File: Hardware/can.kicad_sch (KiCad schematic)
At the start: 11 parts, among them U4 SN65HVD230

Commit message: added jumper to change the buck converter to 8.4v
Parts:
- C33, C35, C36, C37: footprint Capacitor_SMD:C_0603_1608Metric -> Capacitor_SMD:C_0402_1005Metric
- JP1: footprint (none) -> Jumper:SolderJumper-2_P1.3mm_Open_RoundedPad1.0x1.5mm
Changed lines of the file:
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@@
       (effects (font (size 1.27 1.27)) (justify right))
     )
-    (property "Footprint" "Capacitor_SMD:C_0603_1608Metric" (id 2) (at 175.26 82.55 0)
+    (property "Footprint" "Capacitor_SMD:C_0402_1005Metric" (id 2) (at 175.26 82.55 0)
       (effects (font (size 1.27 1.27)) hide)
     )
@@
       (effects (font (size 1.27 1.27)) (justify left))
     )
-    (property "Footprint" "Capacitor_SMD:C_0603_1608Metric" (id 2) (at 121.92 71.12 0)
+    (property "Footprint" "Capacitor_SMD:C_0402_1005Metric" (id 2) (at 121.92 71.12 0)
       (effects (font (size 1.27 1.27)) hide)
     )
@@
     (property "Reference" "C35" (id 0) (at 171.45 82.55 90))
     (property "Value" "0.1uF" (id 1) (at 171.45 85.09 90))
-    (property "Footprint" "Capacitor_SMD:C_0603_1608Metric" (id 2) (at 175.26 87.9348 0)
+    (property "Footprint" "Capacitor_SMD:C_0402_1005Metric" (id 2) (at 175.26 87.9348 0)
       (effects (font (size 1.27 1.27)) hide)
     )
@@
     (property "Reference" "JP1" (id 0) (at 157.48 82.55 0))
     (property "Value" "TermJP" (id 1) (at 157.48 85.09 0))
-    (property "Footprint" "" (id 2) (at 157.48 88.9 0)
+    (property "Footprint" "Jumper:SolderJumper-2_P1.3mm_Open_RoundedPad1.0x1.5mm" (id 2) (at 157.48 88.9 0)
       (effects (font (size 1.27 1.27)) hide)
     )
@@
       (effects (font (size 1.27 1.27)) (justify right))
     )
-    (property "Footprint" "Capacitor_SMD:C_0603_1608Metric" (id 2) (at 175.26 100.33 0)
+    (property "Footprint" "Capacitor_SMD:C_0402_1005Metric" (id 2) (at 175.26 100.33 0)
       (effects (font (size 1.27 1.27)) hide)
     )

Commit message: End of V1
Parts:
- removed JP1: TermJP, Jumper:SolderJumper-2_P1.3mm_Open_RoundedPad1.0x1.5mm, symbol Jumper:SolderJumper_2_Open
- added C32: 160pF, Capacitor_SMD:C_0603_1608Metric, symbol Device:C_Small
- added R26, R27: 90, Resistor_SMD:R_0603_1608Metric, symbol Device:R_Small
- added R33: 0, Resistor_SMD:R_0603_1608Metric, symbol Device:R_Small
- C33, C35, C36, C37: footprint Capacitor_SMD:C_0402_1005Metric -> Capacitor_SMD:C_0603_1608Metric
- R29, R30: footprint Resistor_SMD:R_0603_1608Metric -> Resistor_SMD:R_0805_2012Metric
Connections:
- net CAN_RX: now also R27.1; no longer U4.4 (R)
- net CAN_TX: now also R26.1; no longer U4.1 (D)
- net GND: now also C32.1
- net Vref: now also R33.1
- net at C35.1, R29.2, R30.1: now also R33.2
- new net: C32.2, R26.2, U4.1 (D)
- new net: R27.2, U4.4 (R)
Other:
- moved on the sheet: C33, C34, C35, C36, C37, D12, R29, R30

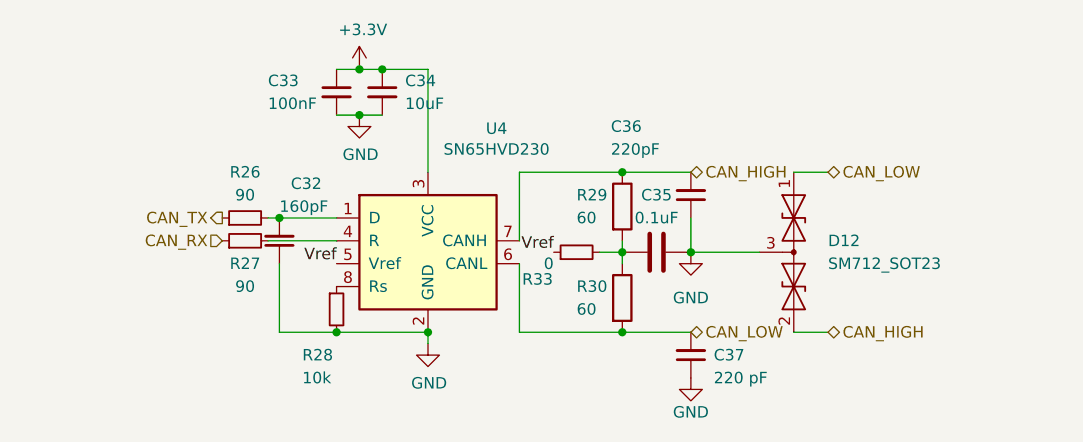
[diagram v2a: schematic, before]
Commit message: mostly completed v2 schematic (pin assignments left)
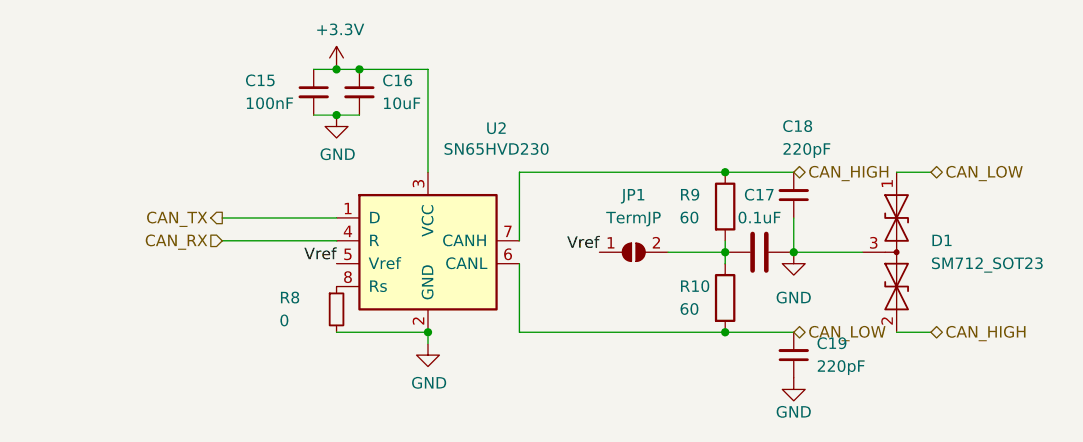
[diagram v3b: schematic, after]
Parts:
- removed C32: 160pF, Capacitor_SMD:C_0603_1608Metric, symbol Device:C_Small
- removed R26, R27: 90, Resistor_SMD:R_0603_1608Metric, symbol Device:R_Small
- removed R33: 0, Resistor_SMD:R_0603_1608Metric, symbol Device:R_Small
- added JP1: TermJP, Jumper:SolderJumper-2_P1.3mm_Open_RoundedPad1.0x1.5mm, symbol Jumper:SolderJumper_2_Open
- C15: renamed from C33; footprint Capacitor_SMD:C_0603_1608Metric -> Capacitor_SMD:C_0402_1005Metric
- C16: renamed from C34; footprint Capacitor_SMD:C_0603_1608Metric -> Capacitor_SMD:C_0402_1005Metric
- C17: renamed from C35; footprint Capacitor_SMD:C_0603_1608Metric -> Capacitor_SMD:C_0402_1005Metric
- C18: renamed from C36; footprint Capacitor_SMD:C_0603_1608Metric -> Capacitor_SMD:C_0402_1005Metric
- C19: renamed from C37; value 220 pF -> 220pF; footprint Capacitor_SMD:C_0603_1608Metric -> Capacitor_SMD:C_0402_1005Metric
- R10: renamed from R30; footprint Resistor_SMD:R_0805_2012Metric -> Resistor_SMD:R_0402_1005Metric
- R8: renamed from R28; value 10k -> 0
- R9: renamed from R29; footprint Resistor_SMD:R_0805_2012Metric -> Resistor_SMD:R_0402_1005Metric
- renumbered D12 to D1, U4 to U2
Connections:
- net CAN_RX: now also U2.4 (R)
- net CAN_TX: now also U2.1 (D)
- net Vref: now also JP1.1 (A)
- net at C17.1, R10.1, R9.2: now also JP1.2 (B)
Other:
- moved on the sheet: C15, C16, C17, C18, C19, D1, R10, R9

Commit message: Mostly completed RBUS side, still buck converter side to do
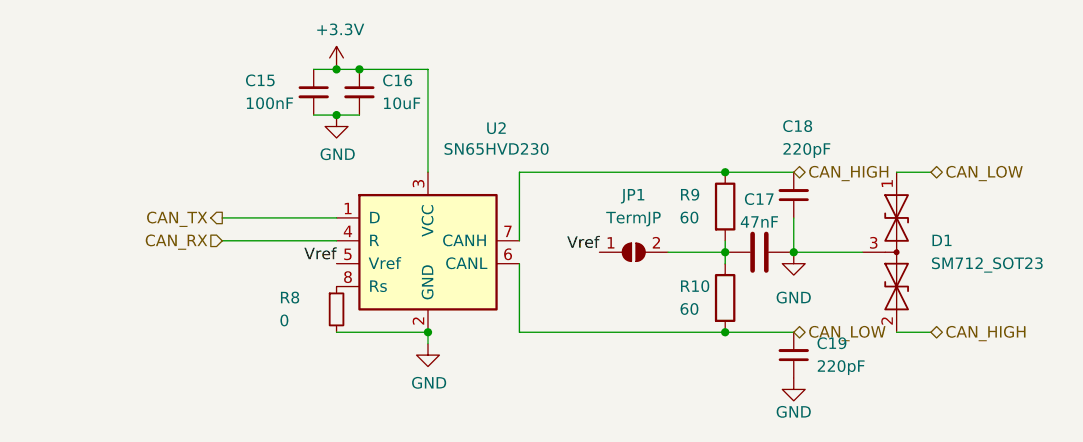
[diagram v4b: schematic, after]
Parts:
- C17: value 0.1uF -> 47nF
- JP1: footprint Jumper:SolderJumper-2_P1.3mm_Open_RoundedPad1.0x1.5mm -> iclr:SmallerSolderJP
- R10, R9: footprint Resistor_SMD:R_0402_1005Metric -> Resistor_SMD:R_0603_1608Metric
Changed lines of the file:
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@@
       (effects (font (size 1.27 1.27)) (justify left))
     )
-    (property "Footprint" "Resistor_SMD:R_0402_1005Metric" (id 2) (at 165.862 93.98 90)
+    (property "Footprint" "Resistor_SMD:R_0603_1608Metric" (id 2) (at 165.862 93.98 90)
       (effects (font (size 1.27 1.27)) hide)
     )
@@
       (effects (font (size 1.27 1.27)) (justify left))
     )
-    (property "Footprint" "Resistor_SMD:R_0402_1005Metric" (id 2) (at 165.862 83.82 90)
+    (property "Footprint" "Resistor_SMD:R_0603_1608Metric" (id 2) (at 165.862 83.82 90)
       (effects (font (size 1.27 1.27)) hide)
     )
@@
   (symbol (lib_id "Device:C") (at 171.45 88.9 90) (unit 1)
     (in_bom yes) (on_board yes) (fields_autoplaced)
-    (property "Reference" "C17" (id 0) (at 171.45 82.55 90))
-    (property "Value" "0.1uF" (id 1) (at 171.45 85.09 90))
+    (property "Reference" "C17" (id 0) (at 171.45 83.0412 90))
+    (property "Value" "47nF" (id 1) (at 171.45 85.5781 90))
     (property "Footprint" "Capacitor_SMD:C_0402_1005Metric" (id 2) (at 175.26 87.9348 0)
       (effects (font (size 1.27 1.27)) hide)
@@
     (property "Reference" "JP1" (id 0) (at 157.48 82.55 0))
     (property "Value" "TermJP" (id 1) (at 157.48 85.09 0))
-    (property "Footprint" "Jumper:SolderJumper-2_P1.3mm_Open_RoundedPad1.0x1.5mm" (id 2) (at 157.48 88.9 0)
+    (property "Footprint" "iclr:SmallerSolderJP" (id 2) (at 157.48 88.9 0)
       (effects (font (size 1.27 1.27)) hide)
     )

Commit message: on the verge of being complete, also updated to kicad 7
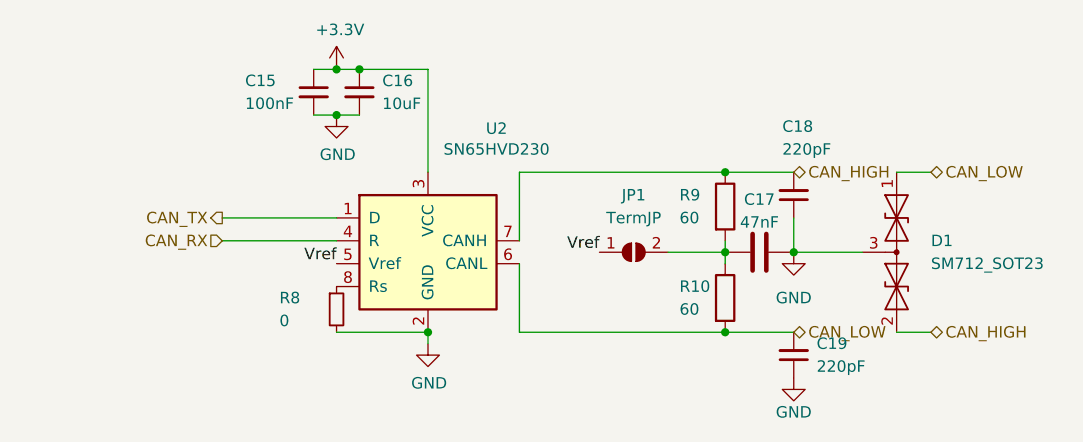
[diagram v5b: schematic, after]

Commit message: all the important stuff routed, only back gfx and via stitch left
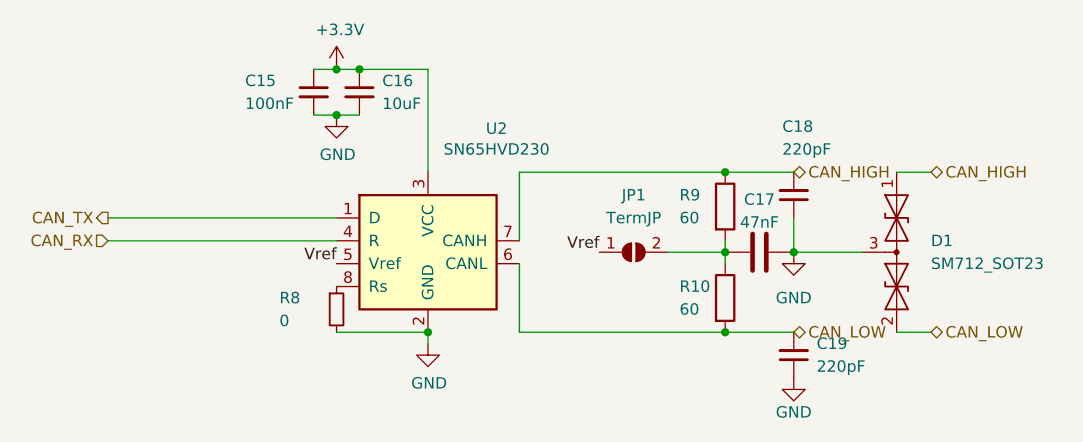
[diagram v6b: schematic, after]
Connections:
- net CAN_HIGH: now also D1.1 (A1); no longer D1.2 (A2)
- net CAN_LOW: now also D1.2 (A2); no longer D1.1 (A1)
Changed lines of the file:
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@@
+    (stroke (width 0) (type default))
+  )
+  (wire (pts (xy 99.06 85.09) (xy 124.46 85.09))
     (stroke (width 0) (type default))
   )
@@
     (stroke (width 0) (type default))
   )
-  (wire (pts (xy 111.76 87.63) (xy 124.46 87.63))
+  (wire (pts (xy 99.06 87.63) (xy 124.46 87.63))
     (stroke (width 0) (type default))
   )
@@
   )
   (wire (pts (xy 186.69 80.01) (xy 190.5 80.01))
-    (stroke (width 0) (type default))
-  )
-  (wire (pts (xy 111.76 85.09) (xy 124.46 85.09))
     (stroke (width 0) (type default))
   )
@@
     (effects (font (size 1.27 1.27)) (justify right bottom))
   )
-  (hierarchical_label "CAN_RX" (shape input) (at 111.76 87.63 180) (fields_autoplaced)
+  (hierarchical_label "CAN_RX" (shape input) (at 99.06 87.63 180) (fields_autoplaced)
     (effects (font (size 1.27 1.27)) (justify right))
   )
@@
     (effects (font (size 1.27 1.27)) (justify left))
   )
-  (hierarchical_label "CAN_TX" (shape output) (at 111.76 85.09 180) (fields_autoplaced)
+  (hierarchical_label "CAN_TX" (shape output) (at 99.06 85.09 180) (fields_autoplaced)
     (effects (font (size 1.27 1.27)) (justify right))
   )
-  (hierarchical_label "CAN_HIGH" (shape bidirectional) (at 190.5 97.79 0) (fields_autoplaced)
+  (hierarchical_label "CAN_HIGH" (shape bidirectional) (at 190.5 80.01 0) (fields_autoplaced)
     (effects (font (size 1.27 1.27)) (justify left))
   )
-  (hierarchical_label "CAN_LOW" (shape bidirectional) (at 190.5 80.01 0) (fields_autoplaced)
+  (hierarchical_label "CAN_LOW" (shape bidirectional) (at 190.5 97.79 0) (fields_autoplaced)
     (effects (font (size 1.27 1.27)) (justify left))
   )

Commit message: took out the can caps
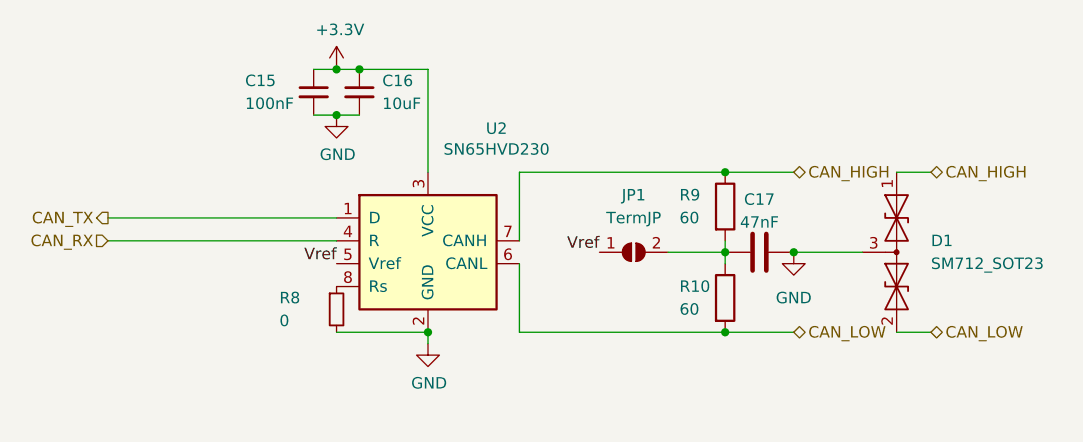
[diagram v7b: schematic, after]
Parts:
- removed C18, C19: 220pF, Capacitor_SMD:C_0402_1005Metric, symbol Device:C_Small
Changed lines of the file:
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@@
-    (stroke (width 0) (type default))
-  )
-  (wire (pts (xy 175.26 85.09) (xy 175.26 88.9))
     (stroke (width 0) (type default))
   )
@@
     )
   )
-  (symbol (lib_id "Device:C_Small") (at 175.26 82.55 180) (unit 1)
-    (in_bom yes) (on_board yes) (dnp no)
-    (property "Reference" "C18" (at 173.99 74.93 0)
-      (effects (font (size 1.27 1.27)) (justify right))
-    )
-    (property "Value" "220pF" (at 173.99 77.47 0)
-      (effects (font (size 1.27 1.27)) (justify right))
-    )
-    (property "Footprint" "Capacitor_SMD:C_0402_1005Metric" (at 175.26 82.55 0)
-      (effects (font (size 1.27 1.27)) hide)
-    )
-    (property "Datasheet" "~" (at 175.26 82.55 0)
-      (effects (font (size 1.27 1.27)) hide)
-    )
-    (pin "1")
-    (pin "2")
-    (instances
-      (project "Chad"
-        (path "/7db990e4-92e1-4f99-b4d2-435bbec1ba83/00000000-0000-0000-0000-000061942b9a"
-          (reference "C18") (unit 1)
-        )
-      )
-    )
-  )
   (symbol (lib_id "Diode:SM712_SOT23") (at 186.69 88.9 270) (unit 1)
     (in_bom yes) (on_board yes) (dnp no) (fields_autoplaced)
@@
         (path "/7db990e4-92e1-4f99-b4d2-435bbec1ba83/00000000-0000-0000-0000-000061942b9a"
           (reference "#PWR033") (unit 1)
-        )
-      )
-    )
-  )
-  (symbol (lib_id "power:GND") (at 175.26 102.87 0) (unit 1)
-    (in_bom yes) (on_board yes) (dnp no) (fields_autoplaced)
-    (property "Reference" "#PWR034" (at 175.26 109.22 0)
-      (effects (font (size 1.27 1.27)) hide)
-    )
-    (property "Value" "GND" (at 175.26 106.68 0)
-      (effects (font (size 1.27 1.27)))
-    )
-    (property "Footprint" "" (at 175.26 102.87 0)
-      (effects (font (size 1.27 1.27)) hide)
-    )
-    (property "Datasheet" "" (at 175.26 102.87 0)
-      (effects (font (size 1.27 1.27)) hide)
-    )
-    (pin "1")
-    (instances
-      (project "Chad"
-        (path "/7db990e4-92e1-4f99-b4d2-435bbec1ba83/00000000-0000-0000-0000-000061942b9a"
-          (reference "#PWR034") (unit 1)
         )
       )
@@
         )
       )
-    )
-  )
-  (symbol (lib_id "Device:C_Small") (at 175.26 100.33 180) (unit 1)
-    (in_bom yes) (on_board yes) (dnp no) (fields_autoplaced)
-    (property "Reference" "C19" (at 177.8 99.0535 0)
-      (effects (font (size 1.27 1.27)) (justify right))
-    )
-    (property "Value" "220pF" (at 177.8 101.5935 0)
-      (effects (font (size 1.27 1.27)) (justify right))
-    )
-    (property "Footprint" "Capacitor_SMD:C_0402_1005Metric" (at 175.26 100.33 0)
-      (effects (font (size 1.27 1.27)) hide)
-    )
-    (property "Datasheet" "~" (at 175.26 100.33 0)
-      (effects (font (size 1.27 1.27)) hide)
-    )
-    (pin "1")
-    (pin "2")
-    (instances
-      (project "Chad"
-        (path "/7db990e4-92e1-4f99-b4d2-435bbec1ba83/00000000-0000-0000-0000-000061942b9a"
-          (reference "C19") (unit 1)
-        )
-      )
